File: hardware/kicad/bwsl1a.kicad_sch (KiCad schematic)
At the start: 0 parts

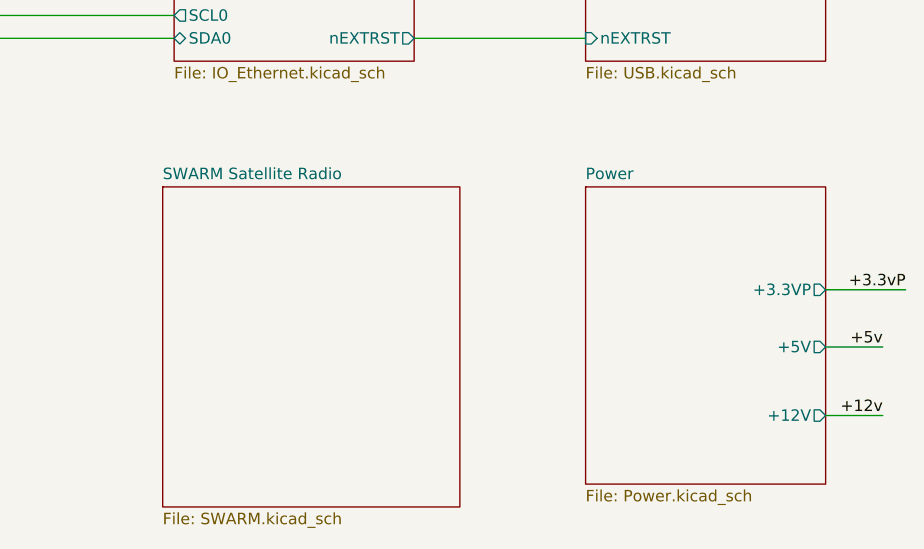
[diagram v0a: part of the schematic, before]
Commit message: update schematic
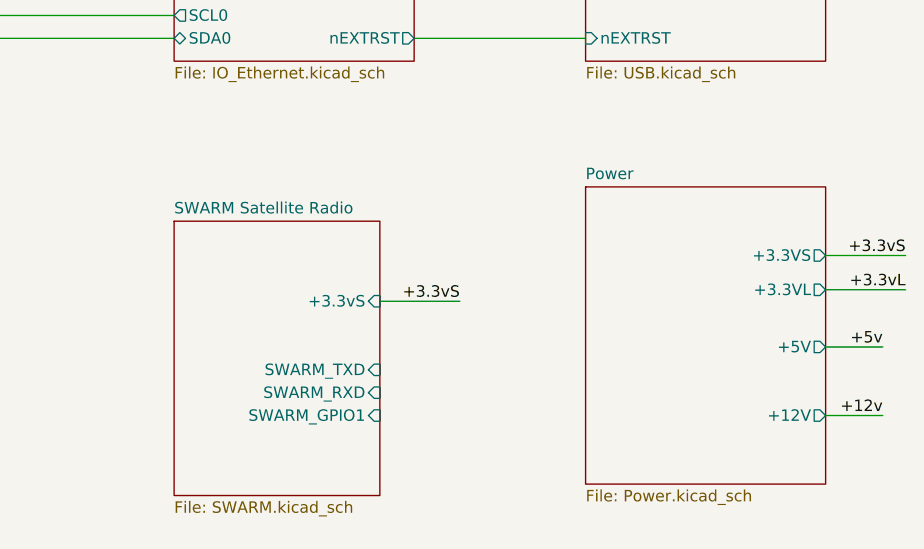
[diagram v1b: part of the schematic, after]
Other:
- sheet Power ports: added +3.3VL, +3.3VS; removed +3.3VP
- sheet SWARM Satellite Radio ports: added +3.3vS, SWARM_GPIO1, SWARM_RXD, SWARM_TXD; removed none
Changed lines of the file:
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@@
+    (stroke (width 0) (type default) (color 0 0 0 0))
+  )
+  (wire (pts (xy 156.21 106.68) (xy 165.1 106.68))
+    (stroke (width 0) (type default) (color 0 0 0 0))
+  )
+  (wire (pts (xy 205.74 101.6) (xy 214.63 101.6))
     (stroke (width 0) (type default) (color 0 0 0 0))
   )
@@
     (effects (font (size 1.27 1.27)) (justify right bottom))
   )
+  (label "+3.3vS" (at 214.63 101.6 180)
+    (effects (font (size 1.27 1.27)) (justify right bottom))
+  )
   (label "+5v" (at 212.09 111.76 180)
     (effects (font (size 1.27 1.27)) (justify right bottom))
@@
     (effects (font (size 1.27 1.27)) (justify right bottom))
   )
-  (label "+3.3vP" (at 214.63 105.41 180)
+  (label "+3.3vL" (at 214.63 105.41 180)
     (effects (font (size 1.27 1.27)) (justify right bottom))
   )
   (label "+3.3v" (at 109.22 41.91 180)
+    (effects (font (size 1.27 1.27)) (justify right bottom))
+  )
+  (label "+3.3vS" (at 165.1 106.68 180)
     (effects (font (size 1.27 1.27)) (justify right bottom))
   )
@@
     )
   )
-  (sheet (at 132.08 93.98) (size 33.02 35.56) (fields_autoplaced)
+  (sheet (at 133.35 97.79) (size 22.86 30.48) (fields_autoplaced)
     (stroke (width 0.1524) (type solid) (color 0 0 0 0))
     (fill (color 0 0 0 0.0000))
-    (property "Sheet name" "SWARM Satellite Radio" (id 0) (at 132.08 93.2684 0)
+    (property "Sheet name" "SWARM Satellite Radio" (id 0) (at 133.35 97.0784 0)
       (effects (font (size 1.27 1.27)) (justify left bottom))
     )
-    (property "Sheet file" "SWARM.kicad_sch" (id 1) (at 132.08 130.1246 0)
+    (property "Sheet file" "SWARM.kicad_sch" (id 1) (at 133.35 128.8546 0)
       (effects (font (size 1.27 1.27)) (justify left top))
+    )
+    (pin "+3.3vS" input (at 156.21 106.68 0)
+      (effects (font (size 1.27 1.27)) (justify right))
+    )
+    (pin "SWARM_GPIO1" input (at 156.21 119.38 0)
+      (effects (font (size 1.27 1.27)) (justify right))
+    )
+    (pin "SWARM_TXD" input (at 156.21 114.3 0)
+      (effects (font (size 1.27 1.27)) (justify right))
+    )
+    (pin "SWARM_RXD" input (at 156.21 116.84 0)
+      (effects (font (size 1.27 1.27)) (justify right))
     )
   )
@@
       (effects (font (size 1.27 1.27)) (justify left top))
     )
-    (pin "+3.3VP" output (at 205.74 105.41 0)
-      (effects (font (size 1.27 1.27)) (justify right))
-    )
     (pin "+5V" output (at 205.74 111.76 0)
       (effects (font (size 1.27 1.27)) (justify right))
     )
     (pin "+12V" output (at 205.74 119.38 0)
+      (effects (font (size 1.27 1.27)) (justify right))
+    )
+    (pin "+3.3VL" output (at 205.74 105.41 0)
+      (effects (font (size 1.27 1.27)) (justify right))
+    )
+    (pin "+3.3VS" output (at 205.74 101.6 0)
       (effects (font (size 1.27 1.27)) (justify right))
     )
@@
       (reference "#PWR?") (unit 1) (value "GND") (footprint "")
     )
-    (path "/5a0cf2af-562f-4c93-aa06-b80080350c15/1df8df08-c7e2-4f3c-b39b-a9747f156209"
-      (reference "#PWR?") (unit 1) (value "+12V") (footprint "")
+    (path "/53b25689-70d8-4bbb-b01a-496a3bae654e/143944a6-be36-4dce-a7a5-17815da10300"
+      (reference "#PWR?") (unit 1) (value "GND") (footprint "")
     )
     (path "/5a0cf2af-562f-4c93-aa06-b80080350c15/1f165a66-0089-4fa1-99dc-7b59845ad63e"
       (reference "#PWR?") (unit 1) (value "GND") (footprint "")
     )
-    (path "/5a0cf2af-562f-4c93-aa06-b80080350c15/21b95bb4-a7bf-4b8c-8872-0da551667ec2"
-      (reference "#PWR?") (unit 1) (value "+3.3VP") (footprint "")
-    )
     (path "/5a0cf2af-562f-4c93-aa06-b80080350c15/24d57497-a3ef-48ac-b759-68c30d1e76b9"
       (reference "#PWR?") (unit 1) (value "GND") (footprint "")
@@
       (reference "#PWR?") (unit 1) (value "GND") (footprint "")
     )
-    (path "/5a0cf2af-562f-4c93-aa06-b80080350c15/45df35ca-0edf-44b6-8e35-4469b48299b6"
-      (reference "#PWR?") (unit 1) (value "+12V") (footprint "")
-    )
-    (path "/5a0cf2af-562f-4c93-aa06-b80080350c15/96523dd2-df3f-45d5-a9b4-c27713aae878"
-      (reference "#PWR?") (unit 1) (value "+5V") (footprint "")
-    )
-    (path "/5a0cf2af-562f-4c93-aa06-b80080350c15/b395ac21-a947-476c-9af3-8ac07a7b0540"
-      (reference "#PWR?") (unit 1) (value "+3.3VP") (footprint "")
+    (path "/53b25689-70d8-4bbb-b01a-496a3bae654e/3f84c37a-93cb-4f8c-bb0c-8e8637e8db67"
+      (reference "#PWR?") (unit 1) (value "GND") (footprint "")
+    )
+    (path "/53b25689-70d8-4bbb-b01a-496a3bae654e/48be64bd-3e77-4260-86d5-66084cd19e69"
+      (reference "#PWR?") (unit 1) (value "GND") (footprint "")
+    )
+    (path "/53b25689-70d8-4bbb-b01a-496a3bae654e/5bd1847b-f9ae-40ea-a4f6-c9e00932982b"
+      (reference "#PWR?") (unit 1) (value "GND") (footprint "")
+    )
+    (path "/d9a0900f-9f4a-4fab-9848-0355cd2da9f6/6e7907d1-4ef4-4b92-87cc-5bd7931298b7"
+      (reference "#PWR?") (unit 1) (value "GND") (footprint "")
+    )
+    (path "/53b25689-70d8-4bbb-b01a-496a3bae654e/7d6f2826-0e8f-4e8f-b34f-688743726314"
+      (reference "#PWR?") (unit 1) (value "GND") (footprint "")
+    )
+    (path "/53b25689-70d8-4bbb-b01a-496a3bae654e/86ff8e93-2383-4f34-b1ba-4e208b81d5c8"
+      (reference "#PWR?") (unit 1) (value "GND") (footprint "")
+    )
+    (path "/d9a0900f-9f4a-4fab-9848-0355cd2da9f6/8cb11619-d6df-4909-80ab-610d9b2e0ee9"
+      (reference "#PWR?") (unit 1) (value "GND") (footprint "")
     )
     (path "/5a0cf2af-562f-4c93-aa06-b80080350c15/d8951179-1e82-4f49-bad7-17c716781c56"
       (reference "#PWR?") (unit 1) (value "GND") (footprint "")
     )
-    (path "/5a0cf2af-562f-4c93-aa06-b80080350c15/d89fe08a-95eb-44d1-acb1-5e392f56dc13"
-      (reference "#PWR?") (unit 1) (value "+5V") (footprint "")
+    (path "/d9a0900f-9f4a-4fab-9848-0355cd2da9f6/d968f631-061c-4d71-b3ce-f906088a7364"
+      (reference "#PWR?") (unit 1) (value "GND") (footprint "")
+    )
+    (path "/d9a0900f-9f4a-4fab-9848-0355cd2da9f6/e01d1800-3a72-48b4-b4ab-f12230363d53"
+      (reference "#PWR?") (unit 1) (value "GND") (footprint "")
+    )
+    (path "/d9a0900f-9f4a-4fab-9848-0355cd2da9f6/e235158e-b68d-4054-b52c-593f5c495051"
+      (reference "#PWR?") (unit 1) (value "GND") (footprint "")
     )
     (path "/5a0cf2af-562f-4c93-aa06-b80080350c15/f00c78a9-a8cf-4363-b451-5314102f6e40"
+      (reference "#PWR?") (unit 1) (value "GND") (footprint "")
+    )
+    (path "/53b25689-70d8-4bbb-b01a-496a3bae654e/f06195c6-bd0b-40ce-988c-5a773f0ac45e"
       (reference "#PWR?") (unit 1) (value "GND") (footprint "")
     )
@@
       (reference "C46") (unit 1) (value "100n") (footprint "Capacitor_SMD:C_0402_1005Metric")
     )
+    (path "/d9a0900f-9f4a-4fab-9848-0355cd2da9f6/0b661521-7314-47f6-9778-c10417dcde1f"
+      (reference "C?") (unit 1) (value "0.1uF") (footprint "")
+    )
+    (path "/53b25689-70d8-4bbb-b01a-496a3bae654e/20f2db1d-792c-4da7-929f-a90692a92a07"
+      (reference "C?") (unit 1) (value "0.1uF") (footprint "")
+    )
+    (path "/53b25689-70d8-4bbb-b01a-496a3bae654e/3b6ef4ca-4965-435e-912a-ffdc5ac5f8de"
+      (reference "C?") (unit 1) (value "10uF") (footprint "")
+    )
+    (path "/53b25689-70d8-4bbb-b01a-496a3bae654e/660df8c2-ebf4-44b5-97ef-a9d7dcc4f998"
+      (reference "C?") (unit 1) (value "100uF") (footprint "")
+    )
+    (path "/53b25689-70d8-4bbb-b01a-496a3bae654e/697ed47b-f13b-41ae-87ba-f6f2b187d22c"
+      (reference "C?") (unit 1) (value "0.1uF") (footprint "")
+    )
+    (path "/53b25689-70d8-4bbb-b01a-496a3bae654e/7472dd6f-0ff6-4107-9b93-e4afb0442c4c"
+      (reference "C?") (unit 1) (value "100uF") (footprint "")
+    )
+    (path "/d9a0900f-9f4a-4fab-9848-0355cd2da9f6/7bd2b559-a091-4a8f-8d75-b3b1e826ac94"
+      (reference "C?") (unit 1) (value "100uF") (footprint "")
+    )
+    (path "/d9a0900f-9f4a-4fab-9848-0355cd2da9f6/a87ba1a9-f043-4c3e-8829-e25bcce87837"
+      (reference "C?") (unit 1) (value "100uF") (footprint "")
+    )
+    (path "/d9a0900f-9f4a-4fab-9848-0355cd2da9f6/b88b1175-f20c-442f-be20-29eac7645b98"
+      (reference "C?") (unit 1) (value "10uF") (footprint "")
+    )
+    (path "/d9a0900f-9f4a-4fab-9848-0355cd2da9f6/d67cd235-ce5d-4b9f-9558-a6f62e1217b3"
+      (reference "C?") (unit 1) (value "0.1uF") (footprint "")
+    )
     (path "/95cb497e-4575-4b60-9280-05bd4e24f5e7/00000000-0000-0000-0000-00005e286645"
       (reference "D1") (unit 1) (value "LED Red") (footprint "LED_SMD:LED_0603_1608Metric")
@@
     )
     (path "/5a0cf2af-562f-4c93-aa06-b80080350c15/8009f347-d94d-4489-a49b-5cbf7d6104e7"
-      (reference "J?") (unit 1) (value "3.3VP Input") (footprint "")
+      (reference "J?") (unit 1) (value "3.3V SWARM Input") (footprint "")
     )
     (path "/5a0cf2af-562f-4c93-aa06-b80080350c15/a961d4a1-7261-49f8-918c-7e9b5cbbd00d"
-      (reference "J?") (unit 1) (value "3.3VP Input") (footprint "")
+      (reference "J?") (unit 1) (value "3.3V LoRaWAN Input") (footprint "")
     )
     (path "/5a0cf2af-562f-4c93-aa06-b80080350c15/e1f7c122-09ea-49e6-9371-414d2acc00c0"

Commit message: update pcb design
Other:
- sheet LoRAWAN Radio ports: added +3.3vL, GPS_RESET, GPS_RXD, GPS_STANDBY, GPS_TXD, LORA_CSN, LORA_GPIO6, LORA_GPIO8, LORA_MISO, LORA_MOSI, LORA_RESET, LORA_SCK; removed none
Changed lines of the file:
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@@
+    (stroke (width 0) (type default) (color 0 0 0 0))
+  )
+  (wire (pts (xy 102.87 97.79) (xy 111.76 97.79))
     (stroke (width 0) (type default) (color 0 0 0 0))
   )
@@
     (effects (font (size 1.27 1.27)) (justify right bottom))
   )
+  (label "+3.3vL" (at 111.76 97.79 180)
+    (effects (font (size 1.27 1.27)) (justify right bottom))
+  )
   (label "+5v" (at 212.09 111.76 180)
     (effects (font (size 1.27 1.27)) (justify right bottom))
@@
       (effects (font (size 1.27 1.27)) (justify right))
     )
-    (pin "SWARM_GPIO1" input (at 156.21 119.38 0)
-      (effects (font (size 1.27 1.27)) (justify right))
-    )
-    (pin "SWARM_TXD" input (at 156.21 114.3 0)
-      (effects (font (size 1.27 1.27)) (justify right))
-    )
     (pin "SWARM_RXD" input (at 156.21 116.84 0)
       (effects (font (size 1.27 1.27)) (justify right))
     )
+    (pin "SWARM_TXD" output (at 156.21 114.3 0)
+      (effects (font (size 1.27 1.27)) (justify right))
+    )
+    (pin "SWARM_GPIO1" bidirectional (at 156.21 119.38 0)
+      (effects (font (size 1.27 1.27)) (justify right))
+    )
   )
   (sheet (at 179.07 93.98) (size 26.67 33.02) (fields_autoplaced)
@@
     (property "Sheet file" "LoRAWAN.kicad_sch" (id 1) (at 69.85 128.8546 0)
       (effects (font (size 1.27 1.27)) (justify left top))
+    )
+    (pin "+3.3vL" input (at 102.87 97.79 0)
+      (effects (font (size 1.27 1.27)) (justify right))
+    )
+    (pin "GPS_RESET" input (at 102.87 121.92 0)
+      (effects (font (size 1.27 1.27)) (justify right))
+    )
+    (pin "GPS_STANDBY" input (at 69.85 114.3 180)
+      (effects (font (size 1.27 1.27)) (justify left))
+    )
+    (pin "GPS_RXD" input (at 69.85 119.38 180)
+      (effects (font (size 1.27 1.27)) (justify left))
+    )
+    (pin "LORA_CSN" input (at 102.87 114.3 0)
+      (effects (font (size 1.27 1.27)) (justify right))
+    )
+    (pin "LORA_MOSI" input (at 102.87 109.22 0)
+      (effects (font (size 1.27 1.27)) (justify right))
+    )
+    (pin "LORA_MISO" output (at 102.87 106.68 0)
+      (effects (font (size 1.27 1.27)) (justify right))
+    )
+    (pin "LORA_SCK" input (at 102.87 111.76 0)
+      (effects (font (size 1.27 1.27)) (justify right))
+    )
+    (pin "GPS_TXD" output (at 69.85 116.84 180)
+      (effects (font (size 1.27 1.27)) (justify left))
+    )
+    (pin "LORA_RESET" input (at 102.87 124.46 0)
+      (effects (font (size 1.27 1.27)) (justify right))
+    )
+    (pin "LORA_GPIO8" bidirectional (at 69.85 99.06 180)
+      (effects (font (size 1.27 1.27)) (justify left))
+    )
+    (pin "LORA_GPIO6" bidirectional (at 69.85 101.6 180)
+      (effects (font (size 1.27 1.27)) (justify left))
     )
   )
@@
       (reference "#PWR?") (unit 1) (value "GND") (footprint "")
     )
+    (path "/d9a0900f-9f4a-4fab-9848-0355cd2da9f6/25d98bd5-ed13-4f7c-b5b6-677fec5d5e5b"
+      (reference "#PWR?") (unit 1) (value "GND") (footprint "")
+    )
     (path "/5a0cf2af-562f-4c93-aa06-b80080350c15/34c77944-86f6-418e-8f94-56fa6d7aa0db"
       (reference "#PWR?") (unit 1) (value "GND") (footprint "")
@@
       (reference "#PWR?") (unit 1) (value "GND") (footprint "")
     )
+    (path "/d9a0900f-9f4a-4fab-9848-0355cd2da9f6/56901b39-cfc3-4023-9e18-e076ce74e121"
+      (reference "#PWR?") (unit 1) (value "GND") (footprint "")
+    )

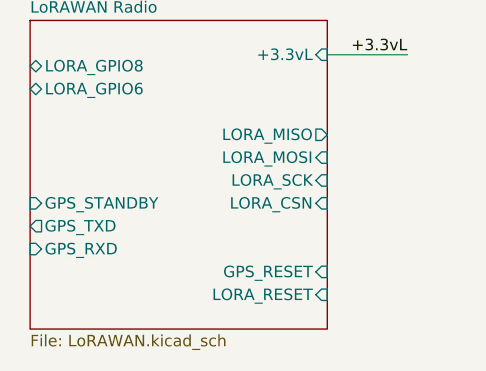
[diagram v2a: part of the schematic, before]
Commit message: breakout GPS I2C
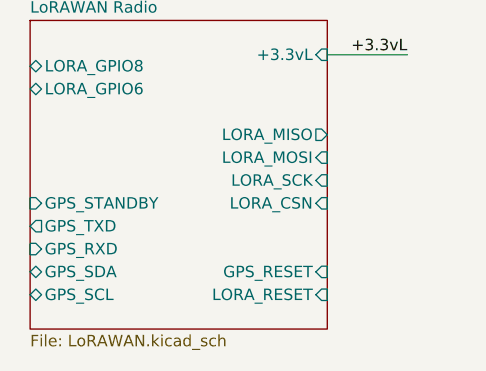
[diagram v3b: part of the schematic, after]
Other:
- sheet LoRAWAN Radio ports: added GPS_SCL, GPS_SDA; removed none
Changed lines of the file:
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@@
+      (effects (font (size 1.27 1.27)) (justify left))
+    )
+    (pin "GPS_SCL" bidirectional (at 69.85 124.46 180)
+      (effects (font (size 1.27 1.27)) (justify left))
+    )
+    (pin "GPS_SDA" bidirectional (at 69.85 121.92 180)
       (effects (font (size 1.27 1.27)) (justify left))
     )

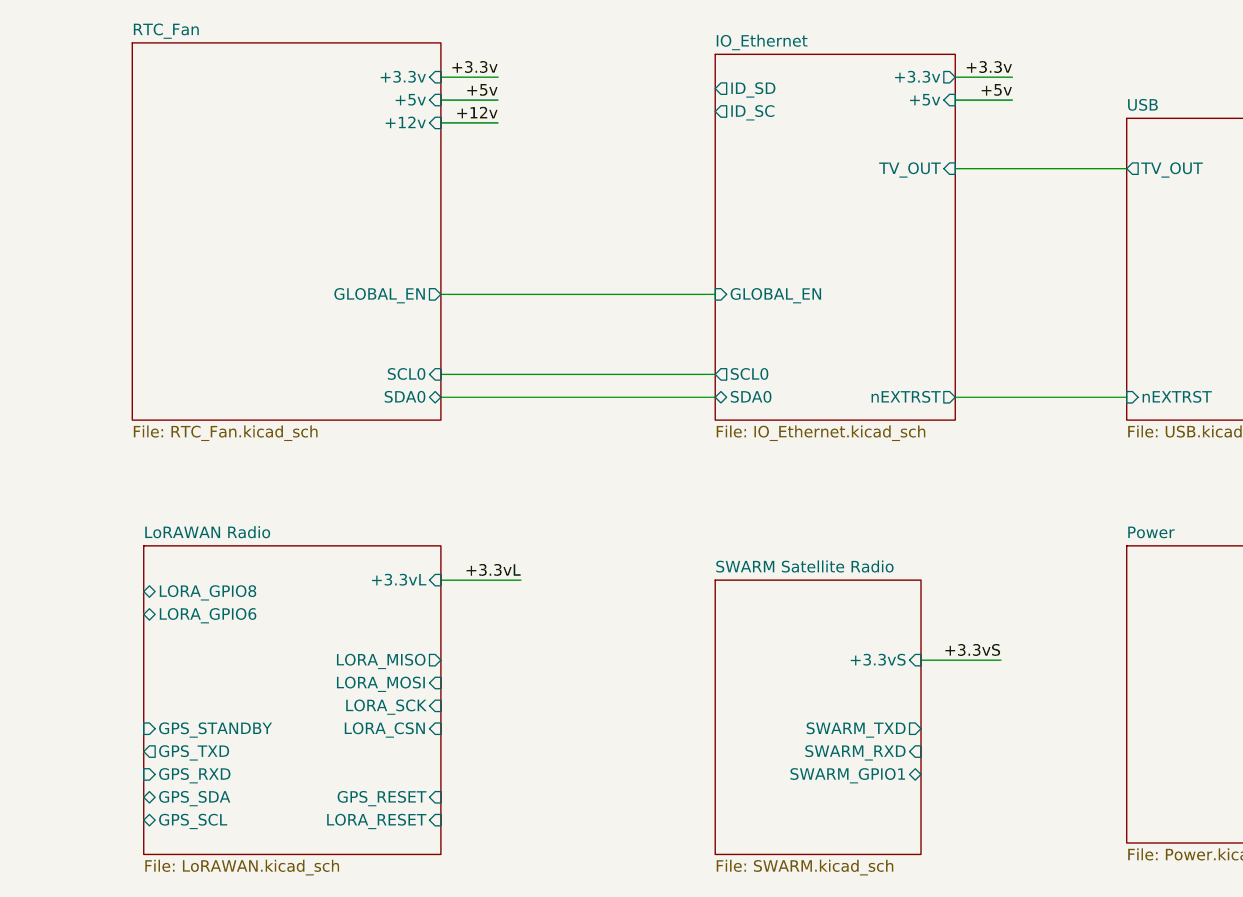
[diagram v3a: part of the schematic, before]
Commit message: wire lorawan and swarm to cm4
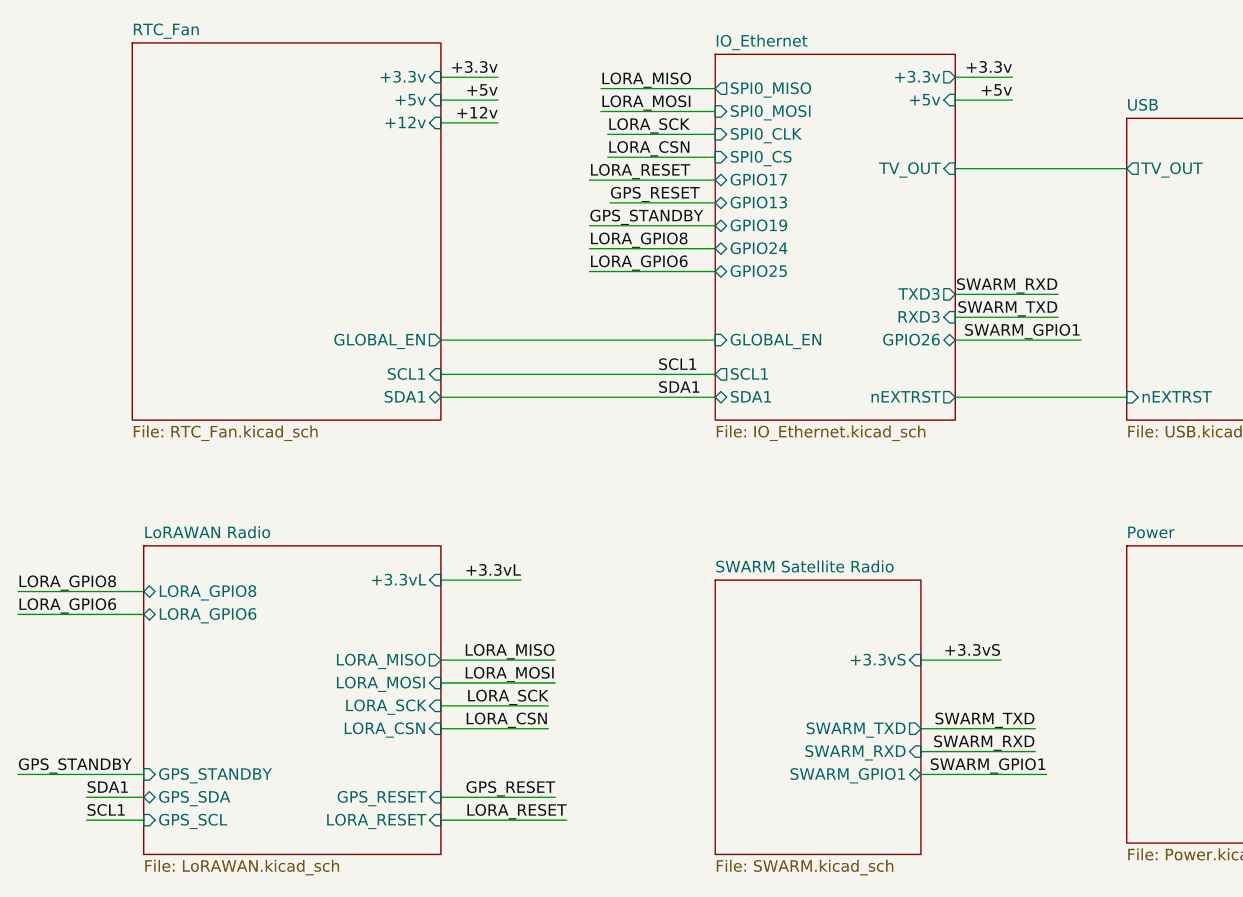
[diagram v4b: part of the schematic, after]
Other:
- sheet IO_Ethernet ports: added GPIO13, GPIO17, GPIO19, GPIO24, GPIO25, GPIO26, RXD3, SCL1, SDA1, SPI0_CLK, SPI0_CS, SPI0_MISO, SPI0_MOSI, TXD3; removed ID_SC, ID_SD, SCL0, SDA0
- sheet LoRAWAN Radio ports: added none; removed GPS_RXD, GPS_TXD
- sheet RTC_Fan ports: added SCL1, SDA1; removed SCL0, SDA0

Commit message: initial pcb design
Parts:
- added H1, H2, H3, H4: MountingHole, MountingHole:MountingHole_3mm_Pad_Via, symbol Mechanical:MountingHole
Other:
- sheet Power ports: added +12v, +3.3vL, +3.3vS, +5v; removed +12V, +3.3VL, +3.3VS, +5V
